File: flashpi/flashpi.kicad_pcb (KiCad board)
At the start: 2 copper layers, 65 x 56.5 mm, 16 parts, among them J1 RPi_GPIO_Compact, SW1 WRITE_PROTECT, SW2 POWER

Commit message: update makefile, minor tweaks
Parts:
- moved SW1 51.1 mm to (184.1, 91.6), turned to 270 degrees
- moved LOGO1 10.9 mm to (144.8, 120.7), turned to 180 degrees
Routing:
- net VCC: track 187.7 -> 62.4 mm
- net /SPI_WP: track 64.2 -> 0.37 mm, vias 2 -> 0
- net /I2C_WP: track 50.0 -> 2.45 mm, vias 1 -> 0
- net /~SPI_CS: track 50.2 -> 13.3 mm
- net /SPI_MOSI: track 64.2 -> 28.2 mm, vias 2 -> 1
- net /SPI_CLK: track 55.5 -> 22.0 mm
- net /SPI_MISO: track 50.3 -> 18.0 mm
- net /I2C_SDA: track 56.3 -> 26.5 mm, vias 1 -> 0
- net /I2C_SCL: track 53.4 -> 26.8 mm
- net GND: vias 31 -> 19

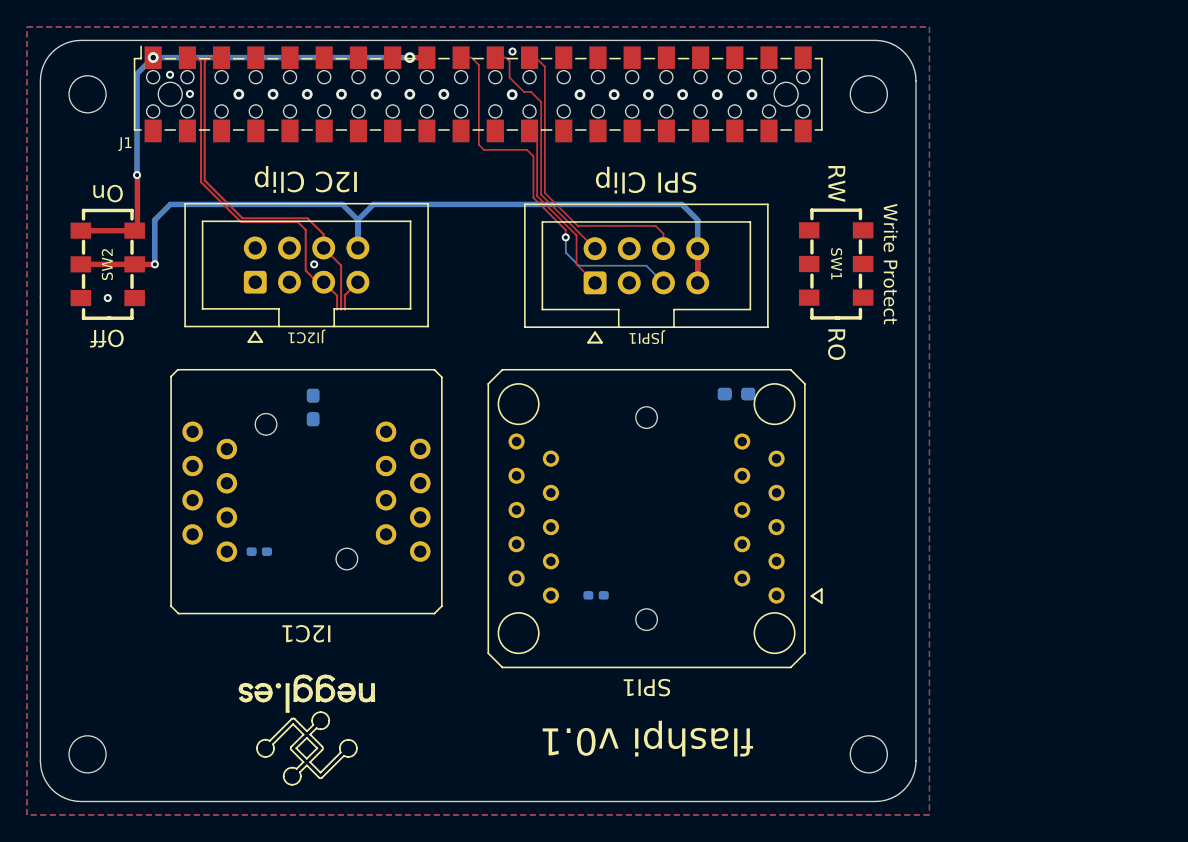
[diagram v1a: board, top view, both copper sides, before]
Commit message: move flashpi to kicad nightly
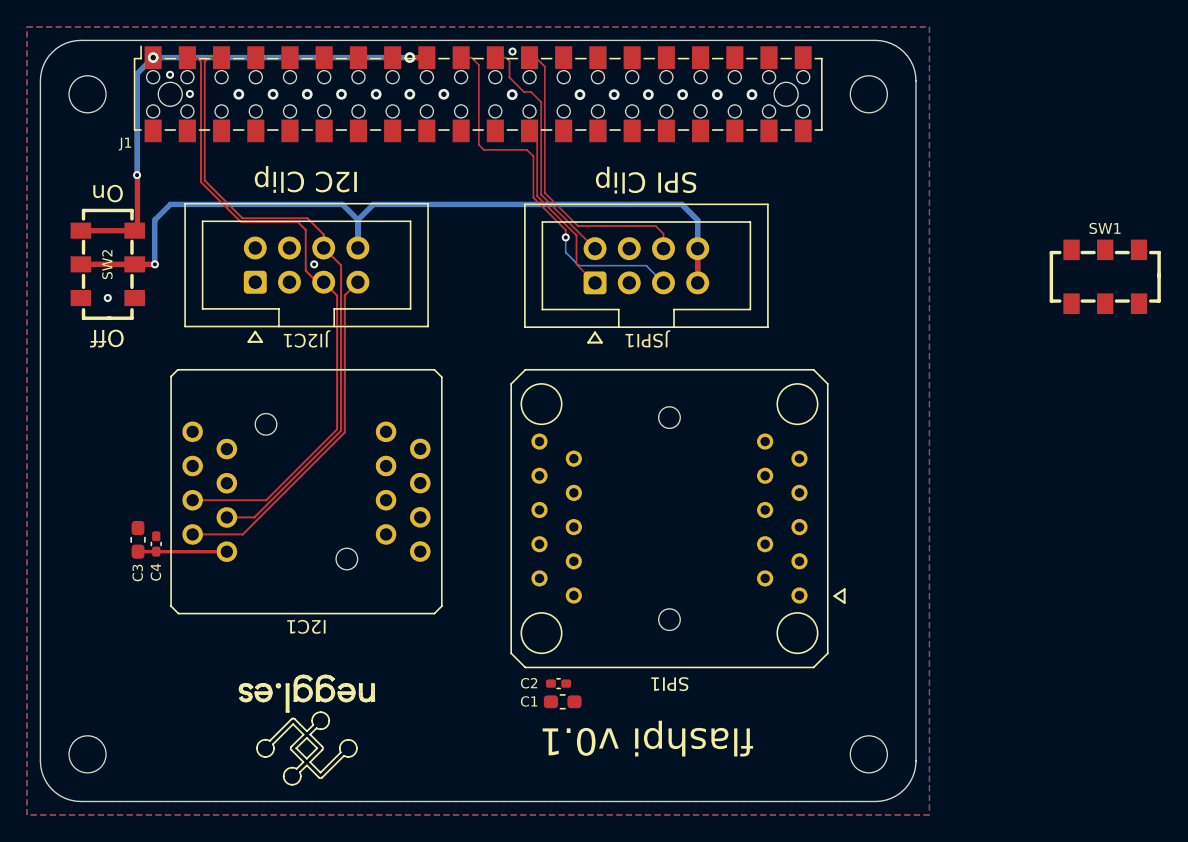
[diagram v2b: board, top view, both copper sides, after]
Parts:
- C1, C2, C3, C4: moved to F.Cu
- moved C1 26.2 mm to (163.8, 124.1)
- moved SW1 20.0 mm to (204.1, 92.5), turned to 0 degrees
- moved C3 16.3 mm to (132.2, 112.1), turned to 90 degrees
- moved C4 7.67 mm to (133.6, 112.4), turned to 90 degrees
- moved C2 7.12 mm to (163.5, 122.8)
- moved SPI1 1.70 mm to (171.7, 110.5)
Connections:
- net /~SPI_CS renamed /~{SPI_CS}
- I2C1 pad 7: /I2C_WP -> /~{WP}
- J1 pad 10: Net-(J1-Pad10) -> (no net)
- J1 pad 11: Net-(J1-Pad11) -> (no net)
- J1 pad 12: Net-(J1-Pad12) -> (no net)
- J1 pad 13: Net-(J1-Pad13) -> (no net)
- J1 pad 15: Net-(J1-Pad15) -> (no net)
- J1 pad 16: Net-(J1-Pad16) -> (no net)
- J1 pad 18: Net-(J1-Pad18) -> (no net)
- J1 pad 2: Net-(J1-Pad2) -> (no net)
- J1 pad 22: Net-(J1-Pad22) -> (no net)
- J1 pad 26: Net-(J1-Pad26) -> (no net)
- J1 pad 27: Net-(J1-Pad27) -> (no net)
- J1 pad 28: Net-(J1-Pad28) -> (no net)
- J1 pad 29: Net-(J1-Pad29) -> (no net)
- J1 pad 31: Net-(J1-Pad31) -> (no net)
- J1 pad 32: Net-(J1-Pad32) -> (no net)
- J1 pad 33: Net-(J1-Pad33) -> (no net)
- J1 pad 35: Net-(J1-Pad35) -> (no net)
- J1 pad 36: Net-(J1-Pad36) -> (no net)
- J1 pad 37: Net-(J1-Pad37) -> (no net)
- J1 pad 38: Net-(J1-Pad38) -> (no net)
- J1 pad 4: Net-(J1-Pad4) -> (no net)
- J1 pad 40: Net-(J1-Pad40) -> (no net)
- J1 pad 7: Net-(J1-Pad7) -> (no net)
- J1 pad 8: Net-(J1-Pad8) -> (no net)
- JI2C1 pad 7: /I2C_WP -> /~{WP}
- JSPI1 pad 3: /SPI_WP -> /~{WP}
- SPI1 pad 3: /SPI_WP -> /~{WP}
- SW1 pad 2: /SPI_WP -> (no net)
- SW1 pad 5: /I2C_WP -> (no net)
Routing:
- net /~{WP}: track 0.00 -> 26.4 mm
- net /I2C_SDA: track 26.5 -> 48.3 mm
- net /I2C_SCL: track 26.8 -> 46.9 mm
- net VCC: track 62.4 -> 69.0 mm
- net /I2C_WP: track 2.45 -> 0.00 mm
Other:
- net class Default removed
- net class USB_D removed
- net class VCC removed
- net class VIN removed
